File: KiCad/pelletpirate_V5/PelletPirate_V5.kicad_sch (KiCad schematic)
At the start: 127 parts, among them J1 SJ1-3523NG_Jack_PP, J2 SJ1-3523NG_Jack_PP, J3 SJ1-3523NG_Jack_PP, J4 SJ1-3523NG_Jack_PP, J5 SJ1-3523NG_Jack_PP, J6 Conn_01x04, J7 Conn_01x04_Socket, J8 USB4105-GF-A_fly, J9 Conn_01x02, T1 BTA12-Triac, T2 BTA12-Triac, T3 BTA12-600BWRG, U1 USBLC6-2SC6, U3 H11AA1M

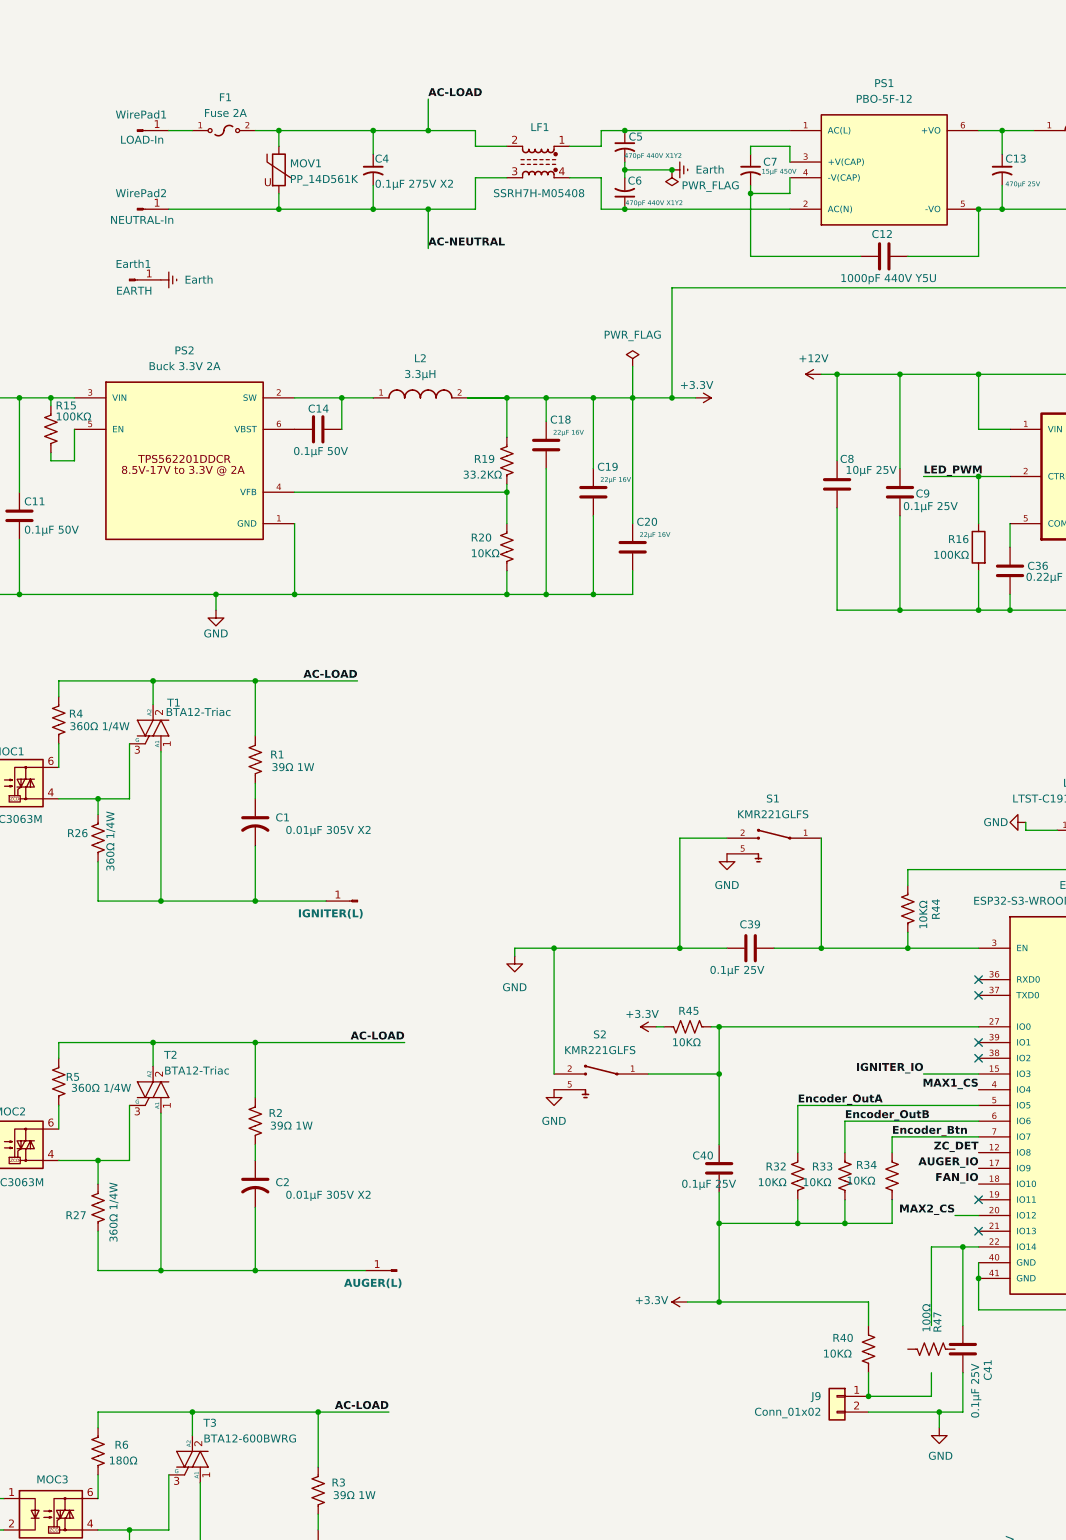
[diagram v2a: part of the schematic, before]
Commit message: V5: net classes + custom DRC rules live; routing underway
Ported V4's 15 net classes with all five dead patterns FIXED (ALL_SCLK,
ALL_SDO, U3-IN2, PS1-+VO, ESP1-* — were silently unmatched typos in V4)
plus new memberships for the snubber midpoints. Created
PelletPirate_V5.kicad_dru: V4's 7 rules incl. the 2.5mm mains-SELV
barrier (values verified against the 2026-07-28 fab archive), with the
U3-IN2 name-crutch clauses removed per the file's own TODO. Netclass-
width routing confirmed working. AC-side placement done; U3 on the
isolation boundary, ZC RC parts near ESP1.

Co-Authored-By: Claude Fable 5 <noreply@anthropic.com>
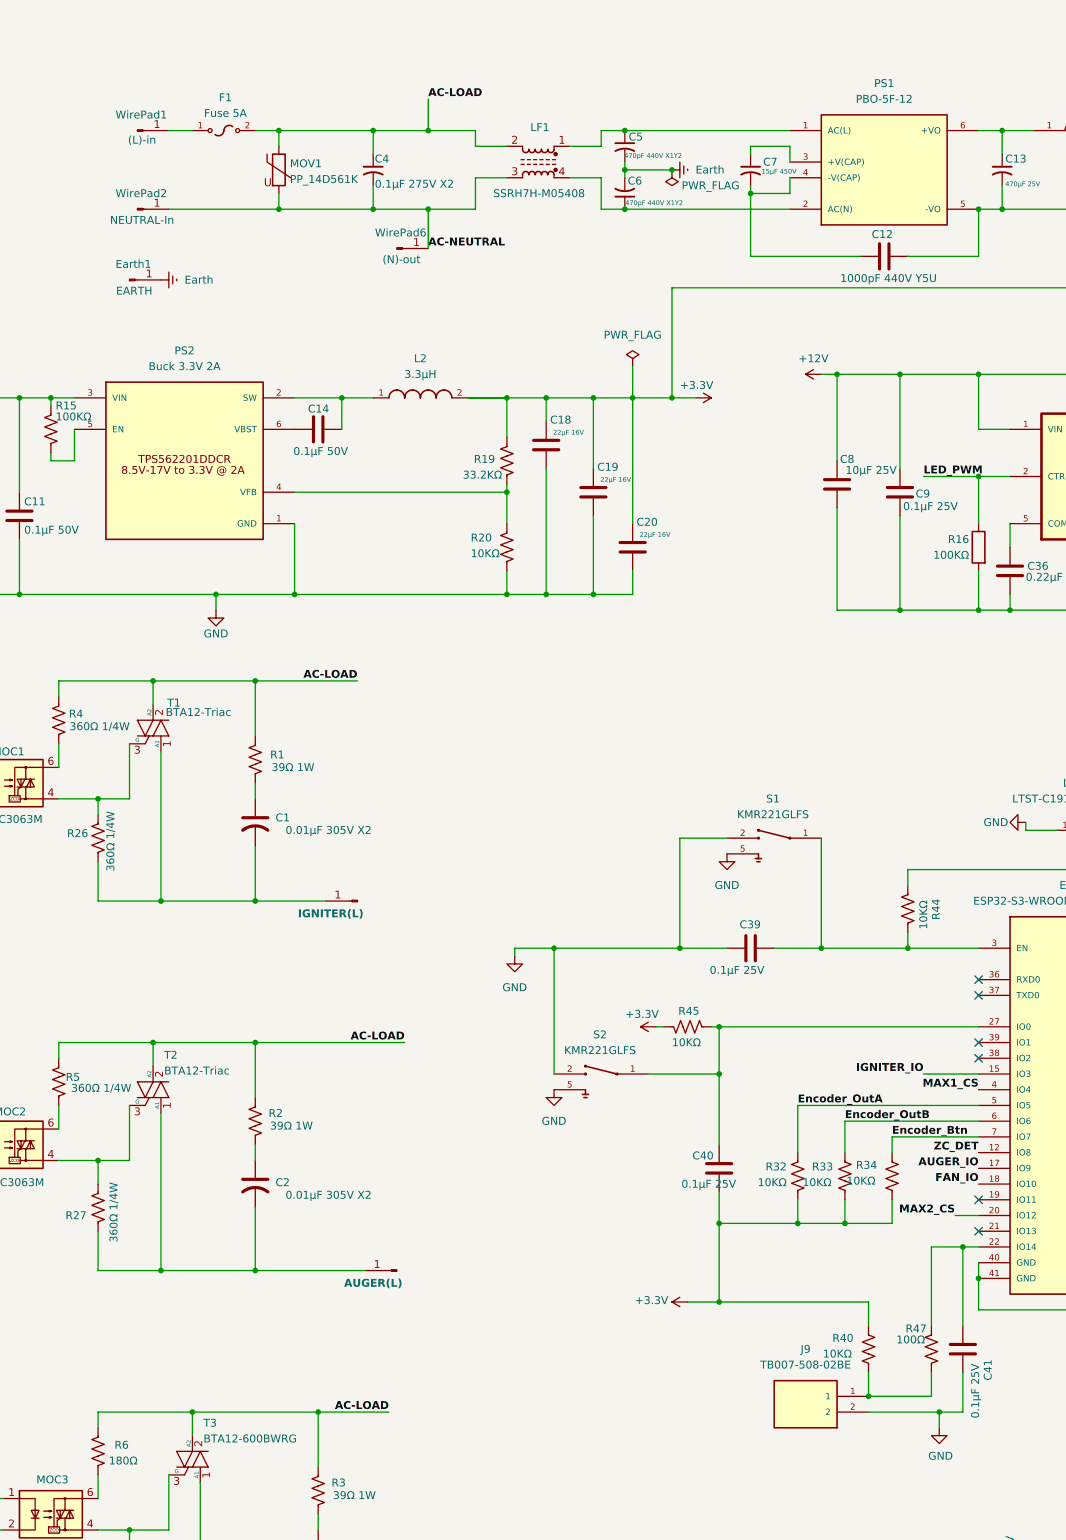
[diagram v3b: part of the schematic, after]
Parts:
- removed J9: Conn_01x02, Connector_Molex:Molex_Micro-Fit_3.0_43650-0215_1x02_P3.00mm_Vertical, symbol Connector_Generic:Conn_01x02
- added J9: TB007-508-02BE, SameSky_Screw_Terminal:CUI_TB007-508-02BE, symbol TB007-508-02BE:TB007-508-02BE
- added WirePad6: (N)-out, Connector_Wire:SolderWire-1.5sqmm_1x01_D1.7mm_OD3mm, symbol Connector:Conn_01x01_Pin
- F1: value Fuse 2A -> Fuse 5A
- WirePad1: value LOAD-In -> (L)-in
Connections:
- net AC-NEUTRAL: now also WirePad6.1 (Pin_1)
- net GND: now also J9.2
- net at C41.2, ESP1.22 (IO14): now also R47.2
- net at R40.2: now also R47.1, J9.1
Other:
- moved on the sheet: R47
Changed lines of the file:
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@@
 	)
 	(junction
-		(at 181.61 238.76)
-		(diameter 0)
-		(color 0 0 0 0)
-	)
-	(junction
 		(at 435.61 204.47)
 		(diameter 0)
@@
 	)
 	(junction
+		(at 181.61 238.76)
+		(diameter 0)
+		(color 0 0 0 0)
+	)
+	(junction
 		(at 82.55 181.61)
 		(diameter 0)
@@
 			)
 		)
-		(property "Value" "Fuse 2A"
+		(property "Value" "Fuse 5A"
 			(at 77.724 31.496 0)
 			(show_name no)
@@
 	)
 	(symbol
-		(lib_id "Connector_Generic:Conn_01x02")
-		(at 176.53 238.76 0)
-		(mirror y)
-		(unit 1)
-		(body_style 1)
-		(exclude_from_sim no)
-		(in_bom yes)
-		(on_board yes)
-		(in_pos_files yes)
-		(dnp no)
-		(property "Reference" "J9"
-			(at 173.99 238.7599 0)
-			(show_name no)
-			(do_not_autoplace no)
-			(effects
-				(font
-					(size 1.27 1.27)
-				)
-				(justify left)
-			)
-		)
-		(property "Value" "Conn_01x02"
-			(at 173.99 241.2999 0)
-			(show_name no)
-			(do_not_autoplace no)
-			(effects
-				(font
-					(size 1.27 1.27)
-				)
-				(justify left)
-			)
-		)
-		(property "Footprint" "Connector_Molex:Molex_Micro-Fit_3.0_43650-0215_1x02_P3.00mm_Vertical"
-			(at 176.53 238.76 0)
-			(hide yes)
-			(show_name no)
-			(do_not_autoplace no)
-			(effects
-				(font
-					(size 1.27 1.27)
-				)
-			)
-		)
-		(property "Datasheet" ""
-			(at 176.53 238.76 0)
-			(hide yes)
-			(show_name no)
-			(do_not_autoplace no)
-			(effects
-				(font
-					(size 1.27 1.27)
-				)
-			)
-		)
-		(property "Description" "Connector Header Through Hole 2 position 0.118\" (3.00mm)"
-			(at 176.53 238.76 0)
-			(hide yes)
-			(show_name no)
-			(do_not_autoplace no)
-			(effects
-				(font
-					(size 1.27 1.27)
-				)
-			)
-		)
-		(property "LINK" "https://www.digikey.com/en/products/detail/molex/0436500215/283461"
-			(at 176.53 238.76 0)
-			(hide yes)
-			(show_name no)
-			(do_not_autoplace no)
-			(effects
-				(font
-					(size 1.27 1.27)
-				)
-			)
-		)
-		(property "MF" "Molex"
-			(at 176.53 238.76 0)
-			(hide yes)
-			(show_name no)
-			(do_not_autoplace no)
-			(effects
-				(font
-					(size 1.27 1.27)
-				)
-			)
-		)
-		(property "MP" "0436500215"
-			(at 176.53 238.76 0)
-			(hide yes)
-			(show_name no)
-			(do_not_autoplace no)
-			(effects
-				(font
-					(size 1.27 1.27)
-				)
-			)
-		)
-		(property "System" "GRILL"
-			(at 176.53 238.76 0)
-			(hide yes)
-			(show_name no)
-			(do_not_autoplace no)
-			(effects
-				(font
-					(size 1.27 1.27)
-				)
-			)
-		)
-		(pin "1"
-		)
-		(pin "2"
-		)
-		(instances
-			(project "PelletPirate_V5"
-				(path "/0182ac56-03c6-4c14-8ead-12e31828f094"
-					(reference "J9")
-					(unit 1)
-				)
-			)
-		)
-	)
-	(symbol
 		(lib_id "Device:C_US")
 		(at 92.71 264.16 0)
@@
 	)
 	(symbol
+		(lib_id "TB007-508-02BE:TB007-508-02BE")
+		(at 171.45 241.3 0)
+		(mirror y)
+		(unit 1)
+		(body_style 1)
+		(exclude_from_sim no)
+		(in_bom yes)
+		(on_board yes)
+		(in_pos_files yes)
+		(dnp no)
+		(fields_autoplaced yes)
+		(property "Reference" "J9"
+			(at 171.45 231.14 0)
+			(show_name no)
+			(do_not_autoplace no)
+			(effects
+				(font
+					(size 1.27 1.27)
+				)
+			)
+		)
+		(property "Value" "TB007-508-02BE"
+			(at 171.45 233.68 0)
+			(show_name no)
+			(do_not_autoplace no)
+			(effects
+				(font
+					(size 1.27 1.27)
+				)
+			)
+		)
+		(property "Footprint" "SameSky_Screw_Terminal:CUI_TB007-508-02BE"
+			(at 171.45 241.3 0)
+			(hide yes)
+			(show_name no)
+			(do_not_autoplace no)
+			(effects
+				(font
+					(size 1.27 1.27)
+				)
+				(justify bottom)
+			)
+		)
+		(property "Datasheet" ""
+			(at 171.45 241.3 0)
+			(hide yes)
+			(show_name no)
+			(do_not_autoplace no)
+			(effects
+				(font
+					(size 1.27 1.27)
+				)
+			)
+		)
+		(property "Description" "2~24 Poles, Screw Type, Horizontal, 5.08 Pitch, 24~12 (AWG), Terminal Block Connector"
+			(at 171.45 241.3 0)
+			(hide yes)
+			(show_name no)
+			(do_not_autoplace no)
+			(effects
+				(font
+					(size 1.27 1.27)
+				)
+				(justify bottom)
+			)
+		)
+		(property "MF" "Same Sky"
+			(at 171.45 241.3 0)
+			(hide yes)
+			(show_name no)
+			(do_not_autoplace no)
+			(effects
+				(font
+					(size 1.27 1.27)
+				)
+				(justify bottom)
+			)
+		)
+		(property "Package" "None"
+			(at 171.45 241.3 0)
+			(hide yes)
+			(show_name no)
+			(do_not_autoplace no)
+			(effects
+				(font
+					(size 1.27 1.27)
+				)
+				(justify bottom)
+			)
+		)
+		(property "Price" "None"
+			(at 171.45 241.3 0)
+			(hide yes)
+			(show_name no)
+			(do_not_autoplace no)
+			(effects
+				(font
+					(size 1.27 1.27)
+				)
+				(justify bottom)
+			)
+		)
+		(property "Check_prices" "https://www.snapeda.com/parts/TB007%20-508-02BE/Same+Sky/view-part/?ref=eda"
+			(at 171.45 241.3 0)
+			(hide yes)
+			(show_name no)
+			(do_not_autoplace no)
+			(effects
+				(font
+					(size 1.27 1.27)
+				)
+				(justify bottom)
+			)
+		)
+		(property "STANDARD" "Manufacturer Recommendations"
+			(at 171.45 241.3 0)
+			(hide yes)
+			(show_name no)
+			(do_not_autoplace no)
+			(effects
+				(font
+					(size 1.27 1.27)
+				)
+				(justify bottom)
+			)
+		)
+		(property "SnapEDA_Link" "https://www.snapeda.com/parts/TB007%20-508-02BE/Same+Sky/view-part/?ref=snap"
+			(at 171.45 241.3 0)
+			(hide yes)
+			(show_name no)
+			(do_not_autoplace no)
+			(effects
+				(font
+					(size 1.27 1.27)
+				)
+				(justify bottom)
+			)
+		)
+		(property "MP" "TB007 -508-02BE"
+			(at 171.45 241.3 0)
+			(hide yes)
+			(show_name no)
+			(do_not_autoplace no)
+			(effects
+				(font
+					(size 1.27 1.27)
+				)
+				(justify bottom)
+			)
+		)
+		(property "Availability" "In Stock"
+			(at 171.45 241.3 0)
+			(hide yes)
+			(show_name no)
+			(do_not_autoplace no)
+			(effects
+				(font
+					(size 1.27 1.27)
+				)
+				(justify bottom)
+			)
+		)
+		(property "MANUFACTURER" "CUI"
+			(at 171.45 241.3 0)
+			(hide yes)
+			(show_name no)
+			(do_not_autoplace no)
+			(effects
+				(font
+					(size 1.27 1.27)
+				)
+				(justify bottom)
+			)
+		)
+		(pin "2"
+		)
+		(pin "1"
+		)
+		(instances
+			(project "PelletPirate_V5"
+				(path "/0182ac56-03c6-4c14-8ead-12e31828f094"
+					(reference "J9")
+					(unit 1)
+				)
+			)
+		)
+	)
+	(symbol
 		(lib_id "Device:R_US")
 		(at 123.19 101.6 0)
@@
 	(symbol
 		(lib_id "Device:R_US")
-		(at 191.77 231.14 270)
+		(at 191.77 231.14 0)
 		(mirror x)
 		(unit 1)
@@
 		(dnp no)
 		(property "Reference" "R47"
-			(at 192.786 225.044 0)
+			(at 191.008 227.838 0)
 			(show_name no)
 			(do_not_autoplace no)
@@
 		)
 		(property "Value" "100Ω"
-			(at 191.008 223.774 0)
+			(at 190.754 229.616 0)
 			(show_name no)
 			(do_not_autoplace no)
@@
 		)
 		(property "Footprint" "Resistor_SMD:R_0402_1005Metric"
-			(at 191.516 230.124 90)
+			(at 192.786 230.886 90)
 			(hide yes)
 			(show_name no)
@@
 	)
 	(symbol
+		(lib_id "Connector:Conn_01x01_Pin")
+		(at 105.41 53.34 0)
+		(unit 1)
+		(body_style 1)
+		(exclude_from_sim no)
+		(in_bom no)
+		(on_board yes)
+		(in_pos_files yes)
+		(dnp no)
+		(property "Reference" "WirePad6"
+			(at 106.045 50.8 0)
+			(show_name no)
+			(do_not_autoplace no)
+			(effects
+				(font
+					(size 1.27 1.27)
+				)
+			)
+		)
+		(property "Value" "(N)-out"
+			(at 106.172 55.118 0)
+			(show_name no)
+			(do_not_autoplace no)
+			(effects
+				(font
+					(size 1.27 1.27)
+				)
+			)
+		)
+		(property "Footprint" "Connector_Wire:SolderWire-1.5sqmm_1x01_D1.7mm_OD3mm"
+			(at 105.41 53.34 0)
+			(hide yes)
+			(show_name no)
+			(do_not_autoplace no)
+			(effects
+				(font
+					(size 1.27 1.27)
+				)
+			)
+		)
+		(property "Datasheet" ""
+			(at 105.41 53.34 0)
+			(hide yes)
+			(show_name no)
+			(do_not_autoplace no)
+			(effects
+				(font
+					(size 1.27 1.27)
+				)
+			)
+		)
+		(property "Description" "Generic connector, single row, 01x01, script generated"
+			(at 105.41 53.34 0)
+			(hide yes)
+			(show_name no)
+			(do_not_autoplace no)
+			(effects
+				(font
+					(size 1.27 1.27)
+				)
+			)
+		)
+		(pin "1"
+		)
+		(instances
+			(project "PelletPirate_V5"
+				(path "/0182ac56-03c6-4c14-8ead-12e31828f094"
+					(reference "WirePad6")
+					(unit 1)
+				)
+			)
+		)
+	)
+	(symbol
 		(lib_id "power:+12V")
 		(at 256.54 34.29 270)
@@
 			)
 		)
-		(property "Value" "LOAD-In"
+		(property "Value" "(L)-in"
 			(at 64.262 35.814 0)
 			(show_name no)

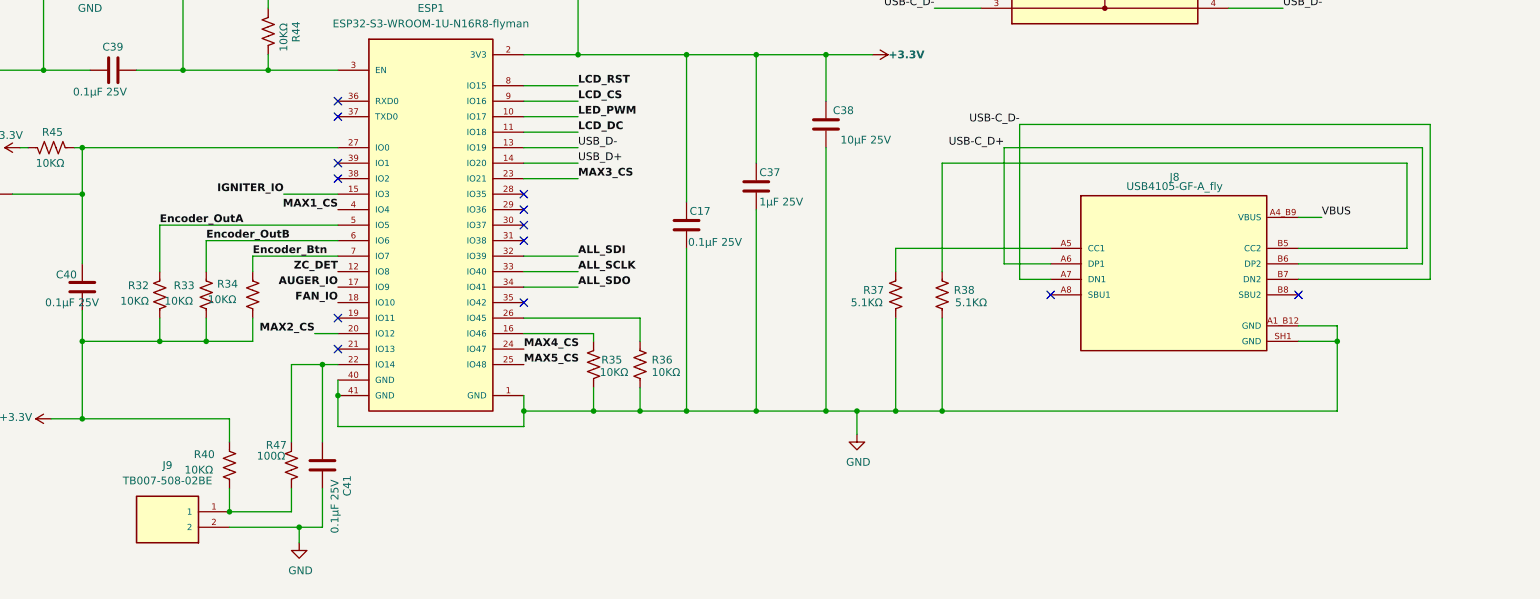
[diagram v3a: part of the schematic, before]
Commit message: V5: connector swaps + MAX CS remap; routing in progress
J8 -> GCT USB4145-03-0070-C vertical USB-C (VBUS_A/B and split data
pins tied per Type-C practice); J9 -> Same Sky TB002-500-02BE 5.00mm
screw terminal (TB007 files replaced with correct TB002 set). MAX CS
lines re-pinned for routing reach: MAX3_CS -> module pad 35 (IO42),
MAX1_CS on a new IO, MAX2/4/5 shuffled among the existing CS GPIOs —
final CS-to-jack map to be extracted from netlist at audit and carried
into boardpins.h as the V5 target delta. 94 DRC violations remain to
triage.

Co-Authored-By: Claude Fable 5 <noreply@anthropic.com>
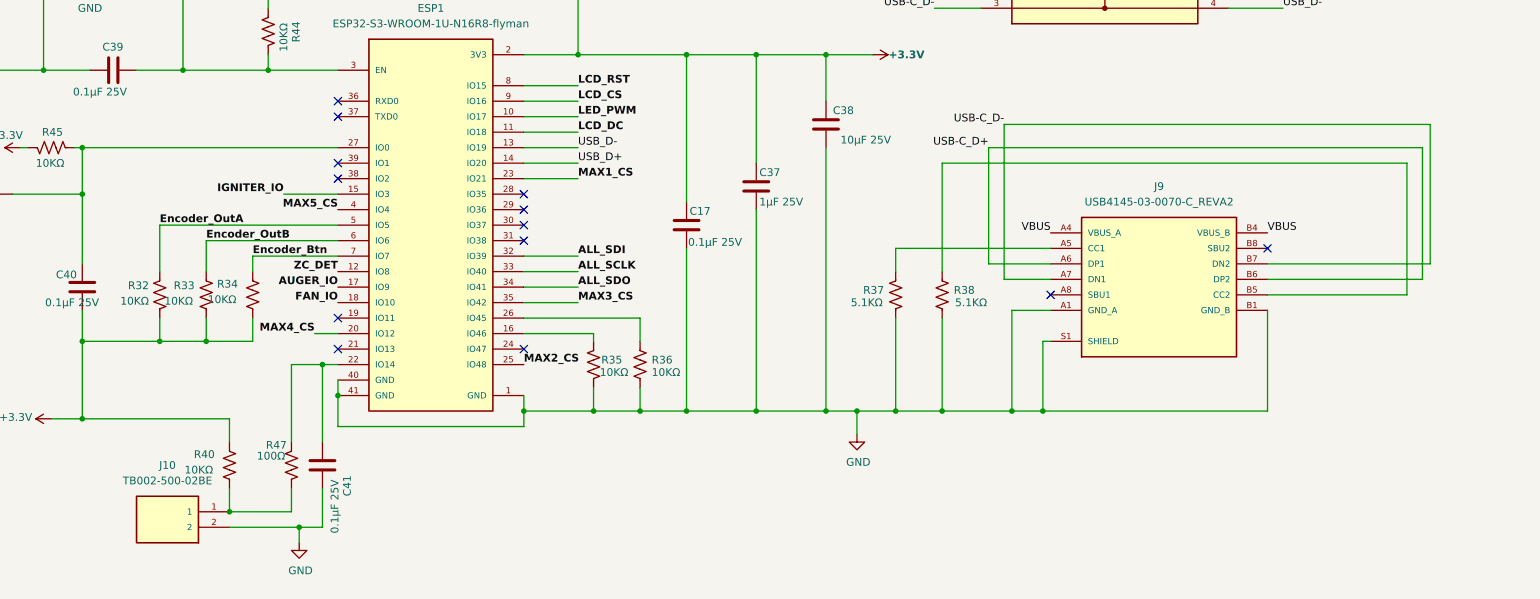
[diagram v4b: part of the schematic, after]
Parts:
- removed J8: USB4105-GF-A_fly, USB_try2:GCT_USB4105-GF-A_flyman, symbol USB4105-GF-A-flyman:USB4105-GF-A_fly
- removed J9: TB007-508-02BE, SameSky_Screw_Terminal:CUI_TB007-508-02BE, symbol TB007-508-02BE:TB007-508-02BE
- added J10: TB002-500-02BE, SameSky_Screw_Terminal:CUI_TB002-500-02BE, symbol TB002-500-02BE:TB002-500-02BE
- added J9: USB4145-03-0070-C_REVA2, USB_try2:GCT_USB4145-03-0070-C_REVA2, symbol USB4145-03-0070-C_REVA2:USB4145-03-0070-C_REVA2
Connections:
- net GND: now also J10.2, J9.A1 (GND_A), J9.A12 (GND_A), J9.B1 (GND_B), J9.B12 (GND_B), J9.S1 (SHIELD), J9.S2 (SHIELD), J9.S3 (SHIELD), J9.S4 (SHIELD)
- net MAX1_CS: now also ESP1.23 (IO21); no longer ESP1.4 (IO4)
- net MAX2_CS: now also ESP1.25 (IO48); no longer ESP1.20 (IO12)
- net MAX3_CS: now also ESP1.35 (IO42); no longer ESP1.23 (IO21)
- net MAX4_CS: now also ESP1.20 (IO12); no longer ESP1.24 (IO47)
- net MAX5_CS: now also ESP1.4 (IO4); no longer ESP1.25 (IO48)
- net USB-C_D+: now also J9.A6 (DP1), J9.B6 (DP2)
- net USB-C_D-: now also J9.A7 (DN1), J9.B7 (DN2)
- net at R40.2, R47.1: now also J10.1
- net at R38.1: now also J9.B5 (CC2)
- net at R37.1: now also J9.A5 (CC1)
- net VBUS renamed VBUS_A
- net VBUS_A: now also J9.A4 (VBUS_A), J9.A9 (VBUS_A), J9.B4 (VBUS_B), J9.B9 (VBUS_B)
